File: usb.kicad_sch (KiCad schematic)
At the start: 5 parts, among them J13 USB-C 2.0, U9 USBLC6-2SC6

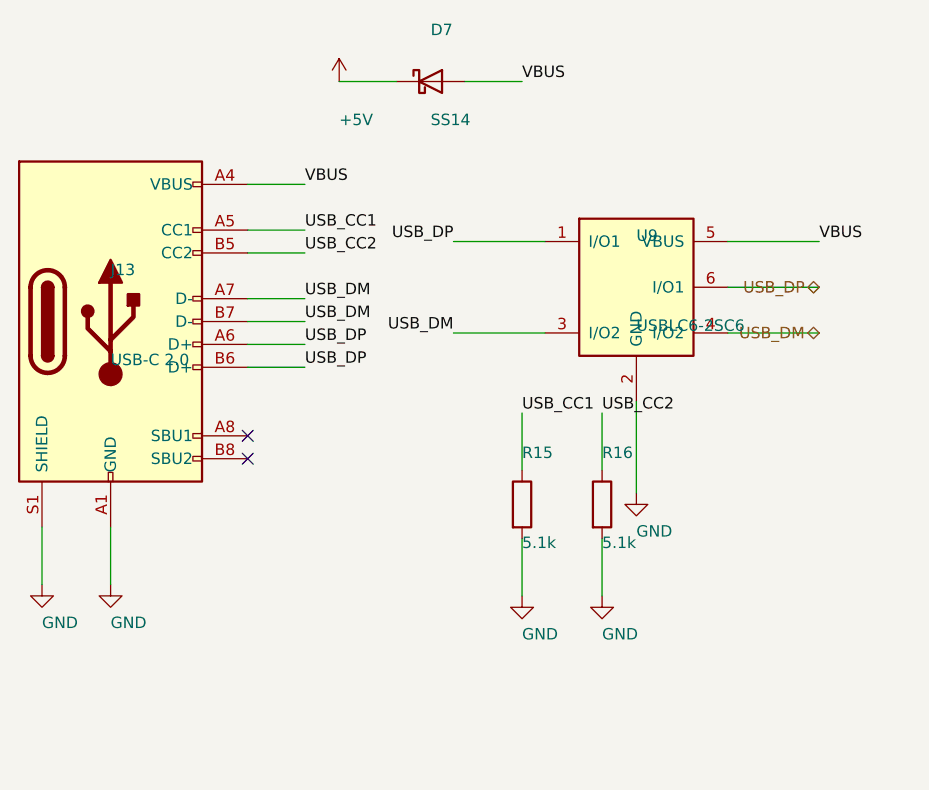
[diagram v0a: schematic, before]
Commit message: WIP: J18/Q2/Q3/R30/R31 + reguardado KiCad de todas las hojas
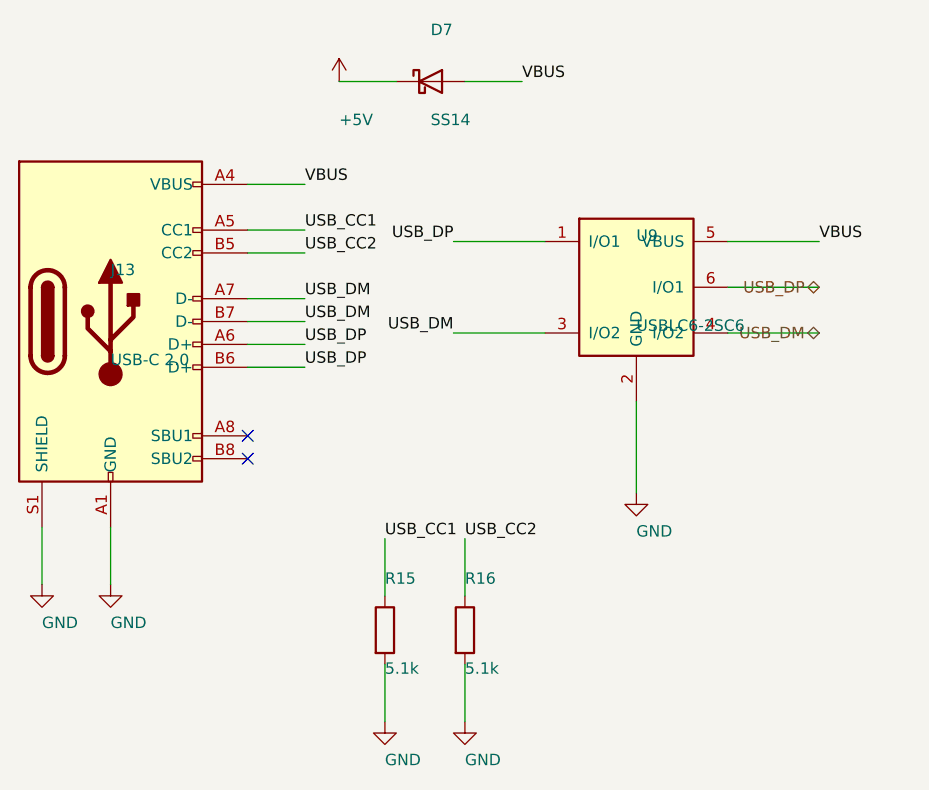
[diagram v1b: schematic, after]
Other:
- moved on the sheet: R15, R16

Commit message: friday changes
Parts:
- D7: DigiKey (none) -> 1655-DSS14UTR-ND
- J13: DigiKey (none) -> 2073-USB4085-GF-ATR-ND
- R15, R16: DigiKey (none) -> RMCF1206JT5K10TR-ND; MPN (none) -> RMCF1206JT5K10; Manufacturer (none) -> Stackpole Electronics Inc
- U9: DigiKey (none) -> 5399-USBLC6-2SC6TR-ND
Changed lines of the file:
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@@
+			)
+		)
+		(property "DigiKey" "2073-USB4085-GF-ATR-ND"
+			(at 0 0 0)
+			(effects
+				(font
+					(size 1.27 1.27)
+				)
+				(hide yes)
 			)
 		)
@@
 			)
 		)
+		(property "Manufacturer" "Stackpole Electronics Inc"
+			(at 0 0 0)
+			(effects
+				(font
+					(size 1.27 1.27)
+				)
+				(hide yes)
+			)
+		)
+		(property "MPN" "RMCF1206JT5K10"
+			(at 0 0 0)
+			(effects
+				(font
+					(size 1.27 1.27)
+				)
+				(hide yes)
+			)
+		)
+		(property "DigiKey" "RMCF1206JT5K10TR-ND"
+			(at 0 0 0)
+			(effects
+				(font
+					(size 1.27 1.27)
+				)
+				(hide yes)
+			)
+		)
 		(pin "1"
 		)
@@
 			)
 		)
+		(property "Manufacturer" "Stackpole Electronics Inc"
+			(at 0 0 0)
+			(effects
+				(font
+					(size 1.27 1.27)
+				)
+				(hide yes)
+			)
+		)
+		(property "MPN" "RMCF1206JT5K10"
+			(at 0 0 0)
+			(effects
+				(font
+					(size 1.27 1.27)
+				)
+				(hide yes)
+			)
+		)
+		(property "DigiKey" "RMCF1206JT5K10TR-ND"
+			(at 0 0 0)
+			(effects
+				(font
+					(size 1.27 1.27)
+				)
+				(hide yes)
+			)
+		)
 		(pin "1"
 		)
@@
 			)
 		)
+		(property "DigiKey" "1655-DSS14UTR-ND"
+			(at 0 0 0)
+			(effects
+				(font
+					(size 1.27 1.27)
+				)
+				(hide yes)
+			)
+		)
 		(pin "1"
 		)
@@
 				(hide yes)
 			)
+		)
+		(property "DigiKey" "5399-USBLC6-2SC6TR-ND"
+			(at 0 0 0)
+			(effects
+				(font
+					(size 1.27 1.27)
+				)
+				(hide yes)
+			)

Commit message: schematic updated
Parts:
- renumbered D7 to D5, J13 to J19, R15 to R28, R16 to R29, U9 to U8
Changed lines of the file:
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@@
 		(on_board yes)
 		(dnp no)
-		(property "Reference" "J13"
+		(property "Reference" "J19"
 			(at 172.72 143.59 0)
 			(effects
@@
 			(project "controlcarreta"
 				(path "/9232987b-e923-413e-abd9-77ced6cc4c47/a9f5f58e-9f19-4b76-92d3-0178cc2d2479"
-					(reference "J13")
+					(reference "J19")
 					(unit 1)
 				)
@@
 		(on_board yes)
 		(dnp no)
-		(property "Reference" "#PWR0522"
+		(property "Reference" "#PWR0156"
 			(at 172.72 172.8 0)
 			(effects
@@
 			(project "controlcarreta"
 				(path "/9232987b-e923-413e-abd9-77ced6cc4c47/a9f5f58e-9f19-4b76-92d3-0178cc2d2479"
-					(reference "#PWR0522")
+					(reference "#PWR0156")
 					(unit 1)
 				)
@@
 		(on_board yes)
 		(dnp no)
-		(property "Reference" "#PWR0523"
+		(property "Reference" "#PWR0155"
 			(at 165.1 172.8 0)
 			(effects
@@
 			(project "controlcarreta"
 				(path "/9232987b-e923-413e-abd9-77ced6cc4c47/a9f5f58e-9f19-4b76-92d3-0178cc2d2479"
-					(reference "#PWR0523")
+					(reference "#PWR0155")
 					(unit 1)
 				)
@@
 		(on_board yes)
 		(dnp no)
-		(property "Reference" "R15"
+		(property "Reference" "R28"
 			(at 203.2 177.88 0)
 			(effects
@@
 			(project "controlcarreta"
 				(path "/9232987b-e923-413e-abd9-77ced6cc4c47/a9f5f58e-9f19-4b76-92d3-0178cc2d2479"
-					(reference "R15")
+					(reference "R28")
 					(unit 1)
 				)
@@
 		(on_board yes)
 		(dnp no)
-		(property "Reference" "#PWR0524"
+		(property "Reference" "#PWR0158"
 			(at 203.2 188.04 0)
 			(effects
@@
 			(project "controlcarreta"
 				(path "/9232987b-e923-413e-abd9-77ced6cc4c47/a9f5f58e-9f19-4b76-92d3-0178cc2d2479"
-					(reference "#PWR0524")
+					(reference "#PWR0158")
 					(unit 1)
 				)
@@
 		(on_board yes)
 		(dnp no)
-		(property "Reference" "R16"
+		(property "Reference" "R29"
 			(at 212.09 177.88 0)
 			(effects
@@
 			(project "controlcarreta"
 				(path "/9232987b-e923-413e-abd9-77ced6cc4c47/a9f5f58e-9f19-4b76-92d3-0178cc2d2479"
-					(reference "R16")
+					(reference "R29")
 					(unit 1)
 				)
@@
 		(on_board yes)
 		(dnp no)
-		(property "Reference" "#PWR0525"
+		(property "Reference" "#PWR0159"
 			(at 212.09 188.04 0)
 			(effects
@@
 			(project "controlcarreta"
 				(path "/9232987b-e923-413e-abd9-77ced6cc4c47/a9f5f58e-9f19-4b76-92d3-0178cc2d2479"
-					(reference "#PWR0525")
+					(reference "#PWR0159")
 					(unit 1)
 				)
@@
 		(on_board yes)
 		(dnp no)
-		(property "Reference" "D7"
+		(property "Reference" "D5"
 			(at 208.28 116.92 0)
 			(effects
@@
 			(project "controlcarreta"
 				(path "/9232987b-e923-413e-abd9-77ced6cc4c47/a9f5f58e-9f19-4b76-92d3-0178cc2d2479"
-					(reference "D7")
+					(reference "D5")
 					(unit 1)
 				)
@@
 		(on_board yes)
 		(dnp no)
-		(property "Reference" "#PWR0526"
+		(property "Reference" "#PWR0157"
 			(at 198.12 116.92 0)
 			(effects
@@
 			(project "controlcarreta"
 				(path "/9232987b-e923-413e-abd9-77ced6cc4c47/a9f5f58e-9f19-4b76-92d3-0178cc2d2479"
-					(reference "#PWR0526")
+					(reference "#PWR0157")
 					(unit 1)
 				)
@@
 		(on_board yes)
 		(dnp no)
-		(property "Reference" "U9"
+		(property "Reference" "U8"
 			(at 231.14 139.78 0)
 			(effects
@@
 			(project "controlcarreta"
 				(path "/9232987b-e923-413e-abd9-77ced6cc4c47/a9f5f58e-9f19-4b76-92d3-0178cc2d2479"
-					(reference "U9")
+					(reference "U8")
 					(unit 1)
 				)
@@
 		(on_board yes)
 		(dnp no)
-		(property "Reference" "#PWR0527"
+		(property "Reference" "#PWR0160"
 			(at 231.14 162.64 0)
 			(effects
@@
 			(project "controlcarreta"
 				(path "/9232987b-e923-413e-abd9-77ced6cc4c47/a9f5f58e-9f19-4b76-92d3-0178cc2d2479"
-					(reference "#PWR0527")
-					(unit 1)
-				)
+					(reference "#PWR0160")
+					(unit 1)
+				)

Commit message: last changes in work
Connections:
- net GND: no longer U8.2 (GND)
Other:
- moved on the sheet: U8
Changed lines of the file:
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@@
 	(hierarchical_label "USB_DP"
 		(shape bidirectional)
-		(at 251.46 144.78 180)
+		(at 251.46 144.78 0)
 		(effects
 			(font
 				(size 1.27 1.27)
 			)
-			(justify right)
+			(justify left)
 		)
 	)
 	(hierarchical_label "USB_DM"
 		(shape bidirectional)
-		(at 251.46 149.86 180)
+		(at 251.46 149.86 0)
 		(effects
 			(font
 				(size 1.27 1.27)
 			)
-			(justify right)
+			(justify left)
 		)
 	)
@@
 		(dnp no)
 		(property "Reference" "U8"
-			(at 231.14 139.78 0)
+			(at 229.87 133.35 0)
 			(effects
 				(font
@@
 		)
 		(property "Value" "USBLC6-2SC6"
-			(at 231.14 149.78 0)
-			(effects
-				(font
-					(size 1.27 1.27)
-				)
-				(justify left bottom)
+			(at 240.03 159.766 0)
+			(effects
+				(font
+					(size 1.27 1.27)
+				)
+				(justify left bottom)
+				(hide yes)
 			)
 		)
@@
 			)
 		)
-		(property "Datasheet" "https://www.digikey.com/en/products/detail/stmicroelectronics/USBLC6-2SC6/1121688"
+		(property "Datasheet" "https://www.digikey.com/en/products/detail/stmicroelectronics/USBLC6-2SC6/1040559"
 			(at 231.14 144.78 0)
 			(effects
